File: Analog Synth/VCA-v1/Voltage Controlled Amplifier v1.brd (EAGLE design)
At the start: 50 x 50 mm, 40 parts, among them IC2 TL084P, IC3 TL084P, IC4 CA3046

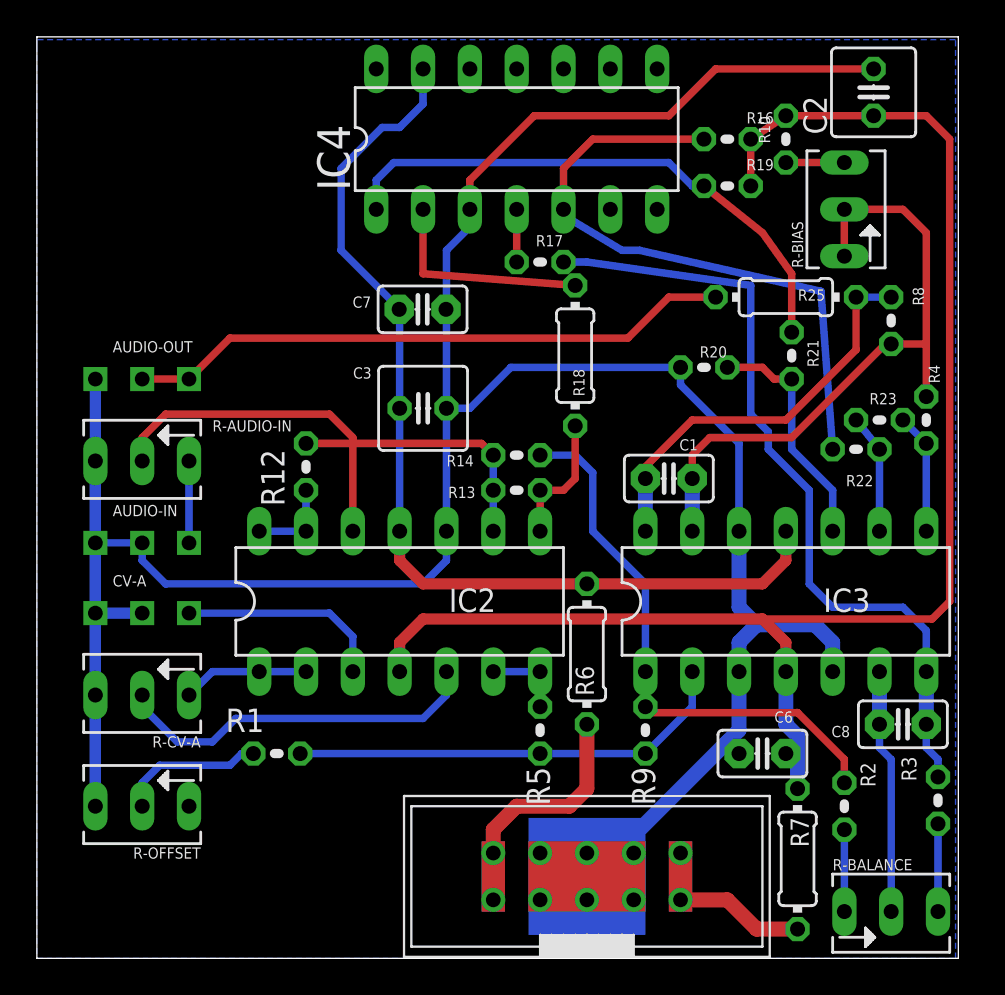
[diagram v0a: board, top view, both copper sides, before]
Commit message: Working on VCA-v1 more. I need to add LED driving circuitry (LEDs, resistors, and a -5V source). Also, the silkscreen for the audio in/out jacks is on the back layer instead of the front. Fix this.
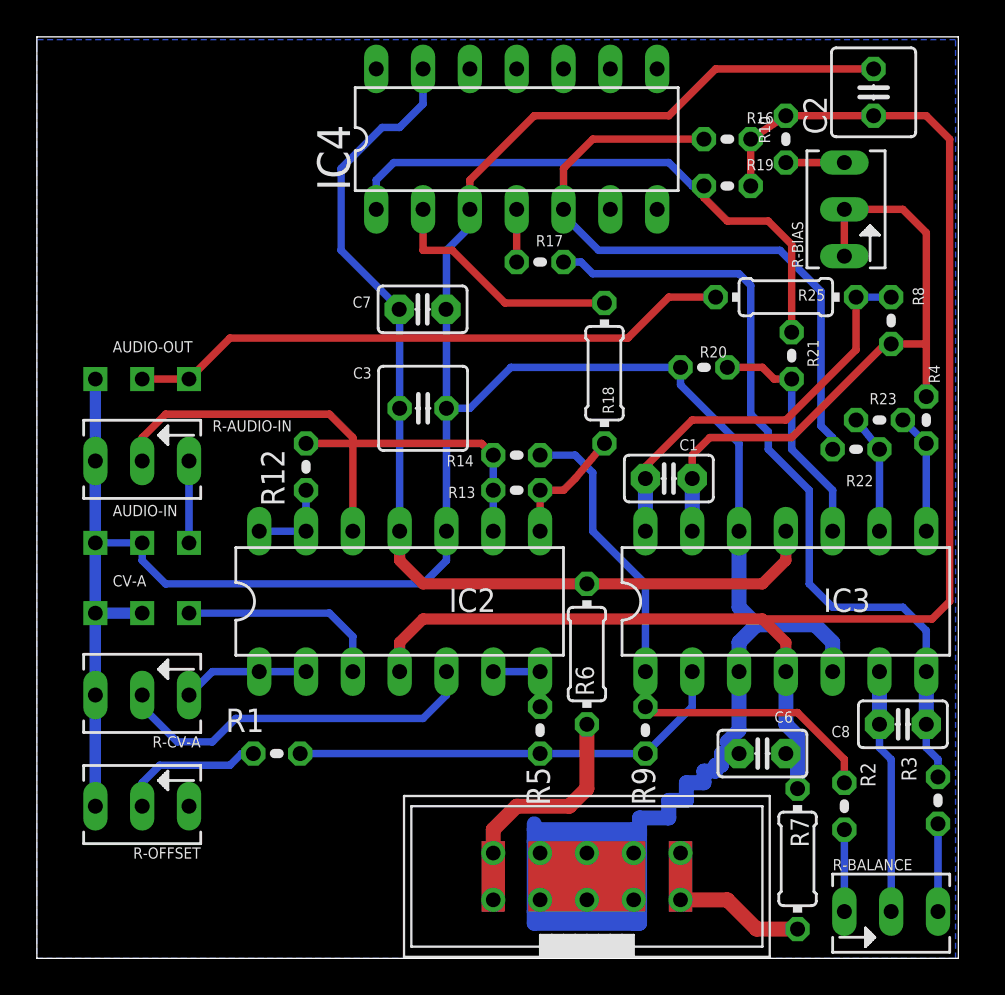
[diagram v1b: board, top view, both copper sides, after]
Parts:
- moved R18 1.85 mm to (30.8, 31.8)
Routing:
- net GND: track 175.3 -> 215.7 mm
- net N$21: track 11.8 -> 13.2 mm
- net N$26: track 30.3 -> 31.5 mm
- net N$24: track 34.2 -> 35.3 mm
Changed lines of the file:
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@@
 <wire x1="50" y1="50" x2="0" y2="50" width="0" layer="20"/>
 <wire x1="0" y1="50" x2="0" y2="0" width="0" layer="20"/>
-<rectangle x1="26.67" y1="1.27" x2="33.02" y2="7.62" layer="16"/>
 </plain>
 <attributes>
@@
 <attribute name="VALUE" x="24.2189" y="38.6461" size="0.6096" layer="27" ratio="10"/>
 </element>
-<element name="R18" library="resistor" package="0204/7" value="10k" x="29.21" y="32.7025" smashed="yes" rot="R270">
-<attribute name="NAME" x="29.1084" y="31.9786" size="0.6096" layer="25" ratio="10" rot="R270"/>
-<attribute name="VALUE" x="28.8036" y="34.8361" size="0.6096" layer="27" ratio="10" rot="R270"/>
+<element name="R18" library="resistor" package="0204/7" value="10k" x="30.7975" y="31.75" smashed="yes" rot="R270">
+<attribute name="NAME" x="30.6959" y="31.0261" size="0.6096" layer="25" ratio="10" rot="R270"/>
+<attribute name="VALUE" x="30.3911" y="33.8836" size="0.6096" layer="27" ratio="10" rot="R270"/>
 </element>
 <element name="R-BALANCE" library="pot" package="B64Y" value="10k Trim" x="46.355" y="2.54"/>
@@
 <wire x1="38.1" y1="23.1775" x2="38.1" y2="19.05" width="0.8128" layer="16"/>
 <wire x1="38.1" y1="19.05" x2="39.0525" y2="18.0975" width="0.8128" layer="16"/>
-<wire x1="32.385" y1="5.715" x2="32.385" y2="6.6675" width="0.8128" layer="16"/>
-<wire x1="32.385" y1="6.6675" x2="37.465" y2="11.7475" width="0.8128" layer="16"/>
 <wire x1="37.465" y1="11.7475" x2="38.1" y2="12.3825" width="0.8128" layer="16"/>
 <wire x1="38.1" y1="12.3825" x2="38.1" y2="15.5575" width="0.8128" layer="16"/>
@@
 <wire x1="27.305" y1="3.175" x2="29.845" y2="3.175" width="0.8128" layer="1"/>
 <wire x1="29.845" y1="3.175" x2="32.385" y2="3.175" width="0.8128" layer="1"/>
-<polygon width="0.4064" layer="16" isolate="1.016">
+<polygon width="0.0254" layer="16" isolate="0.762">
 <vertex x="0" y="49.53"/>
 <vertex x="0" y="0"/>
@@
 <vertex x="0" y="49.8475"/>
 </polygon>
+<wire x1="32.385" y1="5.715" x2="32.385" y2="6.35" width="0.8128" layer="16"/>
+<wire x1="32.385" y1="6.35" x2="32.385" y2="6.6675" width="0.8128" layer="16"/>
+<wire x1="32.385" y1="6.6675" x2="32.385" y2="6.985" width="0.8128" layer="16"/>
+<wire x1="32.385" y1="6.985" x2="26.9875" y2="6.985" width="0.8128" layer="16"/>
+<wire x1="26.9875" y1="6.985" x2="26.9875" y2="6.35" width="0.8128" layer="16"/>
+<wire x1="26.9875" y1="6.35" x2="32.385" y2="6.35" width="0.8128" layer="16"/>
+<wire x1="32.385" y1="6.35" x2="32.7025" y2="6.35" width="0.8128" layer="16"/>
+<wire x1="32.7025" y1="2.54" x2="32.7025" y2="1.905" width="0.8128" layer="16"/>
+<wire x1="26.9875" y1="1.905" x2="26.9875" y2="2.54" width="0.8128" layer="16"/>
+<wire x1="26.9875" y1="2.54" x2="32.7025" y2="2.54" width="0.8128" layer="16"/>
+<wire x1="32.7025" y1="2.54" x2="32.7025" y2="6.35" width="0.8128" layer="16"/>
+<wire x1="32.7025" y1="6.35" x2="32.7025" y2="6.985" width="0.8128" layer="16"/>
+<wire x1="32.7025" y1="6.985" x2="32.385" y2="6.985" width="0.8128" layer="16"/>
+<wire x1="26.9875" y1="6.985" x2="26.9875" y2="7.3025" width="0.8128" layer="16"/>
+<wire x1="26.9875" y1="6.35" x2="26.9875" y2="2.54" width="0.8128" layer="16"/>
+<wire x1="26.9875" y1="1.905" x2="32.385" y2="1.905" width="0.8128" layer="16"/>
+<wire x1="32.7025" y1="1.905" x2="32.385" y2="1.905" width="0.8128" layer="16"/>
+<wire x1="32.385" y1="1.905" x2="32.385" y2="5.715" width="0.8128" layer="16"/>
+<wire x1="32.385" y1="6.6675" x2="32.7025" y2="6.6675" width="0.8128" layer="16"/>
+<wire x1="32.7025" y1="6.6675" x2="32.7025" y2="7.62" width="0.8128" layer="16"/>
+<wire x1="32.7025" y1="7.62" x2="34.29" y2="7.62" width="0.8128" layer="16"/>
+<wire x1="34.29" y1="7.62" x2="34.29" y2="8.5725" width="0.8128" layer="16"/>
+<wire x1="34.29" y1="8.5725" x2="35.2425" y2="8.5725" width="0.8128" layer="16"/>
+<wire x1="35.2425" y1="8.5725" x2="35.2425" y2="9.525" width="0.8128" layer="16"/>
+<wire x1="35.2425" y1="9.525" x2="36.195" y2="9.525" width="0.8128" layer="16"/>
+<wire x1="36.195" y1="9.525" x2="36.195" y2="10.16" width="0.8128" layer="16"/>
+<wire x1="36.195" y1="10.16" x2="36.83" y2="10.16" width="0.8128" layer="16"/>
+<wire x1="36.83" y1="10.16" x2="36.83" y2="10.4775" width="0.8128" layer="16"/>
+<wire x1="36.83" y1="10.4775" x2="37.1475" y2="10.4775" width="0.8128" layer="16"/>
+<wire x1="37.1475" y1="10.4775" x2="37.1475" y2="11.1125" width="0.8128" layer="16"/>
+<wire x1="37.1475" y1="11.1125" x2="38.1" y2="11.1125" width="0.8128" layer="16"/>
 </signal>
 <signal name="+12V">
@@
 <wire x1="48.26" y1="11.43" x2="48.26" y2="12.7" width="0.4064" layer="16"/>
 <contactref element="R17" pad="2"/>
-<wire x1="28.575" y1="37.7825" x2="29.845" y2="37.7825" width="0.4064" layer="16"/>
-<wire x1="29.845" y1="37.7825" x2="38.735" y2="36.5125" width="0.4064" layer="16"/>
+<wire x1="28.575" y1="37.7825" x2="29.5275" y2="37.7825" width="0.4064" layer="16"/>
+<wire x1="29.5275" y1="37.7825" x2="30.1625" y2="37.1475" width="0.4064" layer="16"/>
+<wire x1="30.1625" y1="37.1475" x2="38.1" y2="37.1475" width="0.4064" layer="16"/>
+<wire x1="38.1" y1="37.1475" x2="38.735" y2="36.5125" width="0.4064" layer="16"/>
 <wire x1="38.735" y1="36.5125" x2="38.735" y2="29.5275" width="0.4064" layer="16"/>
 <wire x1="38.735" y1="29.5275" x2="39.6875" y2="28.575" width="0.4064" layer="16"/>
@@
 <contactref element="R18" pad="1"/>
 <contactref element="IC4" pad="2"/>
-<wire x1="20.955" y1="40.64" x2="20.955" y2="37.1475" width="0.4064" layer="1"/>
-<wire x1="20.955" y1="37.1475" x2="29.21" y2="36.5125" width="0.4064" layer="1"/>
+<wire x1="20.955" y1="40.64" x2="20.955" y2="38.4175" width="0.4064" layer="1"/>
+<wire x1="20.955" y1="38.4175" x2="22.5425" y2="38.4175" width="0.4064" layer="1"/>
+<wire x1="22.5425" y1="38.4175" x2="25.4" y2="35.56" width="0.4064" layer="1"/>
+<wire x1="25.4" y1="35.56" x2="30.7975" y2="35.56" width="0.4064" layer="1"/>
 </signal>
 <signal name="N$25">
@@
 <contactref element="R18" pad="2"/>
 <wire x1="27.305" y1="25.4" x2="27.305" y2="23.1775" width="0.4064" layer="1"/>
-<wire x1="29.21" y1="28.8925" x2="29.21" y2="26.035" width="0.4064" layer="1"/>
+<wire x1="30.7975" y1="27.94" x2="29.21" y2="26.035" width="0.4064" layer="1"/>
 <wire x1="29.21" y1="26.035" x2="28.575" y2="25.4" width="0.4064" layer="1"/>
 <wire x1="28.575" y1="25.4" x2="27.305" y2="25.4" width="0.4064" layer="1"/>
@@
 <wire x1="30.1625" y1="44.45" x2="36.195" y2="44.45" width="0.4064" layer="1"/>
 <wire x1="28.575" y1="40.64" x2="28.575" y2="40.3225" width="0.4064" layer="16"/>
-<wire x1="28.575" y1="40.3225" x2="31.75" y2="38.4175" width="0.4064" layer="16"/>
-<wire x1="31.75" y1="38.4175" x2="32.7025" y2="38.4175" width="0.4064" layer="16"/>
-<wire x1="32.7025" y1="38.4175" x2="42.545" y2="36.195" width="0.4064" layer="16"/>
-<wire x1="42.545" y1="36.195" x2="43.18" y2="27.6225" width="0.4064" layer="16"/>
+<wire x1="28.575" y1="40.3225" x2="30.48" y2="38.4175" width="0.4064" layer="16"/>
+<wire x1="30.48" y1="38.4175" x2="40.3225" y2="38.4175" width="0.4064" layer="16"/>
+<wire x1="40.3225" y1="38.4175" x2="42.545" y2="36.195" width="0.4064" layer="16"/>
+<wire x1="42.545" y1="36.195" x2="42.545" y2="28.8925" width="0.4064" layer="16"/>
+<wire x1="42.545" y1="28.8925" x2="43.18" y2="28.2575" width="0.4064" layer="16"/>
+<wire x1="43.18" y1="28.2575" x2="43.18" y2="27.6225" width="0.4064" layer="16"/>
 </signal>
 <signal name="N$26">
@@
 <wire x1="34.29" y1="43.18" x2="35.56" y2="41.91" width="0.4064" layer="16"/>
 <wire x1="35.56" y1="41.91" x2="36.195" y2="41.91" width="0.4064" layer="16"/>
-<wire x1="36.195" y1="41.91" x2="39.37" y2="39.37" width="0.4064" layer="1"/>
-<wire x1="39.37" y1="39.37" x2="40.9575" y2="37.1475" width="0.4064" layer="1"/>
-<wire x1="40.9575" y1="37.1475" x2="40.9575" y2="33.9725" width="0.4064" layer="1"/>
+<wire x1="36.195" y1="41.91" x2="36.195" y2="41.275" width="0.4064" layer="1"/>
+<wire x1="36.195" y1="41.275" x2="37.465" y2="40.005" width="0.4064" layer="1"/>
+<wire x1="37.465" y1="40.005" x2="39.6875" y2="40.005" width="0.4064" layer="1"/>
+<wire x1="39.6875" y1="40.005" x2="40.9575" y2="38.735" width="0.4064" layer="1"/>
+<wire x1="40.9575" y1="38.735" x2="40.9575" y2="33.9725" width="0.4064" layer="1"/>
 </signal>
 <signal name="N$28">

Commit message: working on VCA-v1
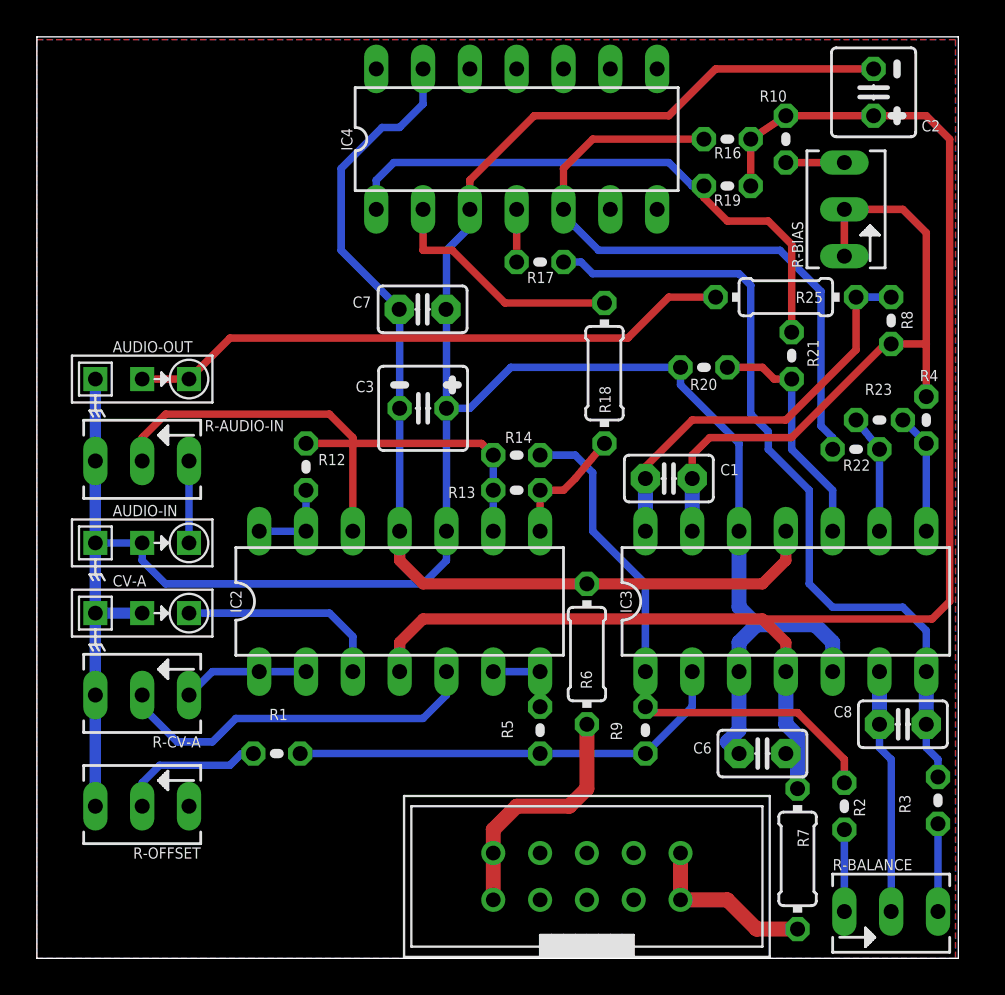
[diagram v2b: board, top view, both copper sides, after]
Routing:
- net GND: track 215.7 -> 154.4 mm
- added copper zone on layer 1, net GND

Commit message: working on VCA more. added caps to filter RF by shunting high frequencies to ground.
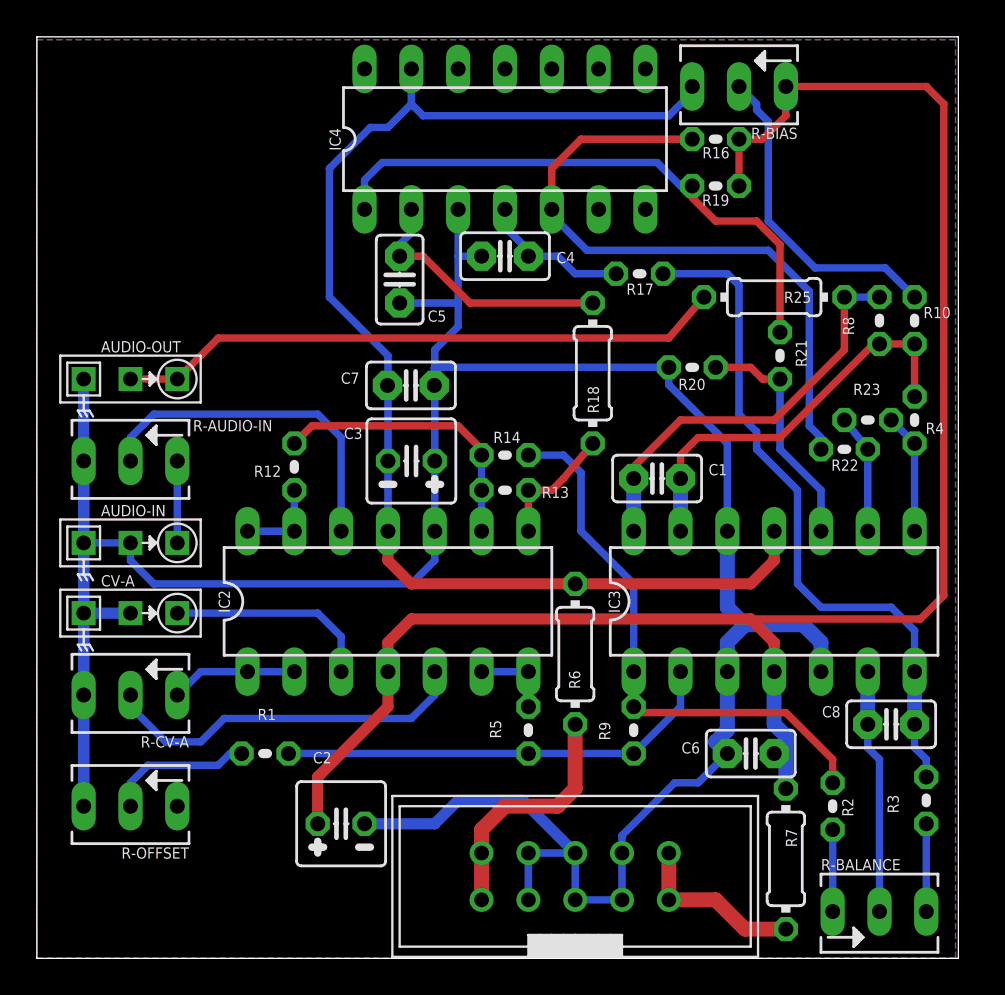
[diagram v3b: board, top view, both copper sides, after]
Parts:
- added C4, C5: 390p, capacitor-wima:C2.5-2
- C1, C8: value 471pf -> 470p
- moved C2 49.1 mm to (16.5, 7.30), turned to 0 degrees
- moved R10 12.1 mm to (47.6, 34.6), turned to 270 degrees
- moved R-BIAS 8.78 mm to (38.1, 47.3), turned to 180 degrees
- moved R17 5.43 mm to (32.7, 37.1)
- moved C7 4.18 mm to (20.3, 31.1)
- moved C3 2.93 mm to (20.3, 27.0)
- moved C8 0.64 mm to (46.4, 12.7)
- moved R16 0.64 mm to (36.8, 44.5)
- moved R19 0.64 mm to (36.8, 41.9)
- moved R21 0.64 mm to (40.3, 32.7)
- moved R22 0.64 mm to (43.8, 27.6)
- moved R3 0.64 mm to (48.3, 8.57)
- moved R9 0.64 mm to (32.4, 12.4)
- moved IC4 0.64 mm to (25.4, 44.5)
- moved R13 0.64 mm to (25.4, 25.4)
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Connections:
- removed net N$16: R-BIAS.A, R10.1
- new net N$11: R-BIAS.S, R10.1
- net +12V: now also R-BIAS.E; no longer R10.2
- net -12V: now also R-BIAS.A
- net GND: now also C4.1, C5.2
- net N$2: now also C4.2
- net N$20: now also R10.2; no longer R-BIAS.E, R-BIAS.S
- net N$21: now also C5.1
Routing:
- net N$11: track 0.00 -> 17.6 mm
- net -12V: track 54.8 -> 71.1 mm
- net +12V: track 82.6 -> 96.4 mm
- net N$20: track 35.7 -> 22.2 mm
- net GND: track 154.4 -> 167.3 mm
- net N$23: track 43.8 -> 37.5 mm
- net N$2: track 2.86 -> 8.22 mm
- net N$16: track 3.17 -> 0.00 mm
- net N$21: track 13.2 -> 14.3 mm
- net N$22: track 14.6 -> 15.5 mm

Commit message: "Finished" VCA-v1. Ordered PCBs from dirtypcbs.com.
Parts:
- added C10: 10µ, rcl:C025-050X050
- added IC1: 79L05, linear:TO92
- added LED-CV: TLLG4400, led:LED3MM
- added R15: 10k, resistor:0204V
- added R24: 22k, resistor:0204V
- moved R-OFFSET 1.59 mm to (5.08, 9.84)
- moved C4 1.27 mm to (24.1, 38.1)
- moved C3 0.95 mm to (20.3, 27.9)
- moved C7 0.66 mm to (20.3, 31.8)
- moved C5 0.64 mm to (20.3, 36.8)
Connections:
- removed net 5V-REG: R-OFFSET.E
- new net -5V: C10.2, IC1.3, LED-CV.K
- new net N$12: LED-CV.A, R15.1
- new net N$49: R-OFFSET.E, R24.1
- net +12V: now also R24.2
- net -12V: now also IC1.2
- net GND: now also C10.1, IC1.1
- net N$1: now also R15.2
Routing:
- net N$1: track 4.45 -> 45.8 mm, vias 0 -> 1
- net GND: track 167.3 -> 197.6 mm
- net -5V: track 0.00 -> 7.33 mm
- net N$12: track 0.00 -> 3.91 mm
- net N$49: track 0.00 -> 2.93 mm
- net +12V: track 96.4 -> 93.4 mm
- net -12V: track 71.1 -> 73.3 mm, vias 0 -> 1
- net N$19: track 18.8 -> 17.6 mm
- net N$21: track 14.3 -> 13.4 mm
- net N$6: track 24.2 -> 25.0 mm
- net N$2: track 8.22 -> 8.97 mm
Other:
- board text added: "2015"
- board text added: "Ryan Jensen"
- board text added: "VCA-v1"
